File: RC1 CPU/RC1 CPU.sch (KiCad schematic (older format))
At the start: 42 parts, among them J1 Expansion, J2 RC1_UI_Port, J3 BARREL_JACK, M1 Mounting, M2 Mounting, M3 Mounting, M4 Mounting, U1 WD65C02, U2 HM62256BLP-7, U3 28C256, U4 6532, U5 74LS00, U6 LM556, U7 74LS145, U8 74LS138, U9 74LS00, X1 1MHz

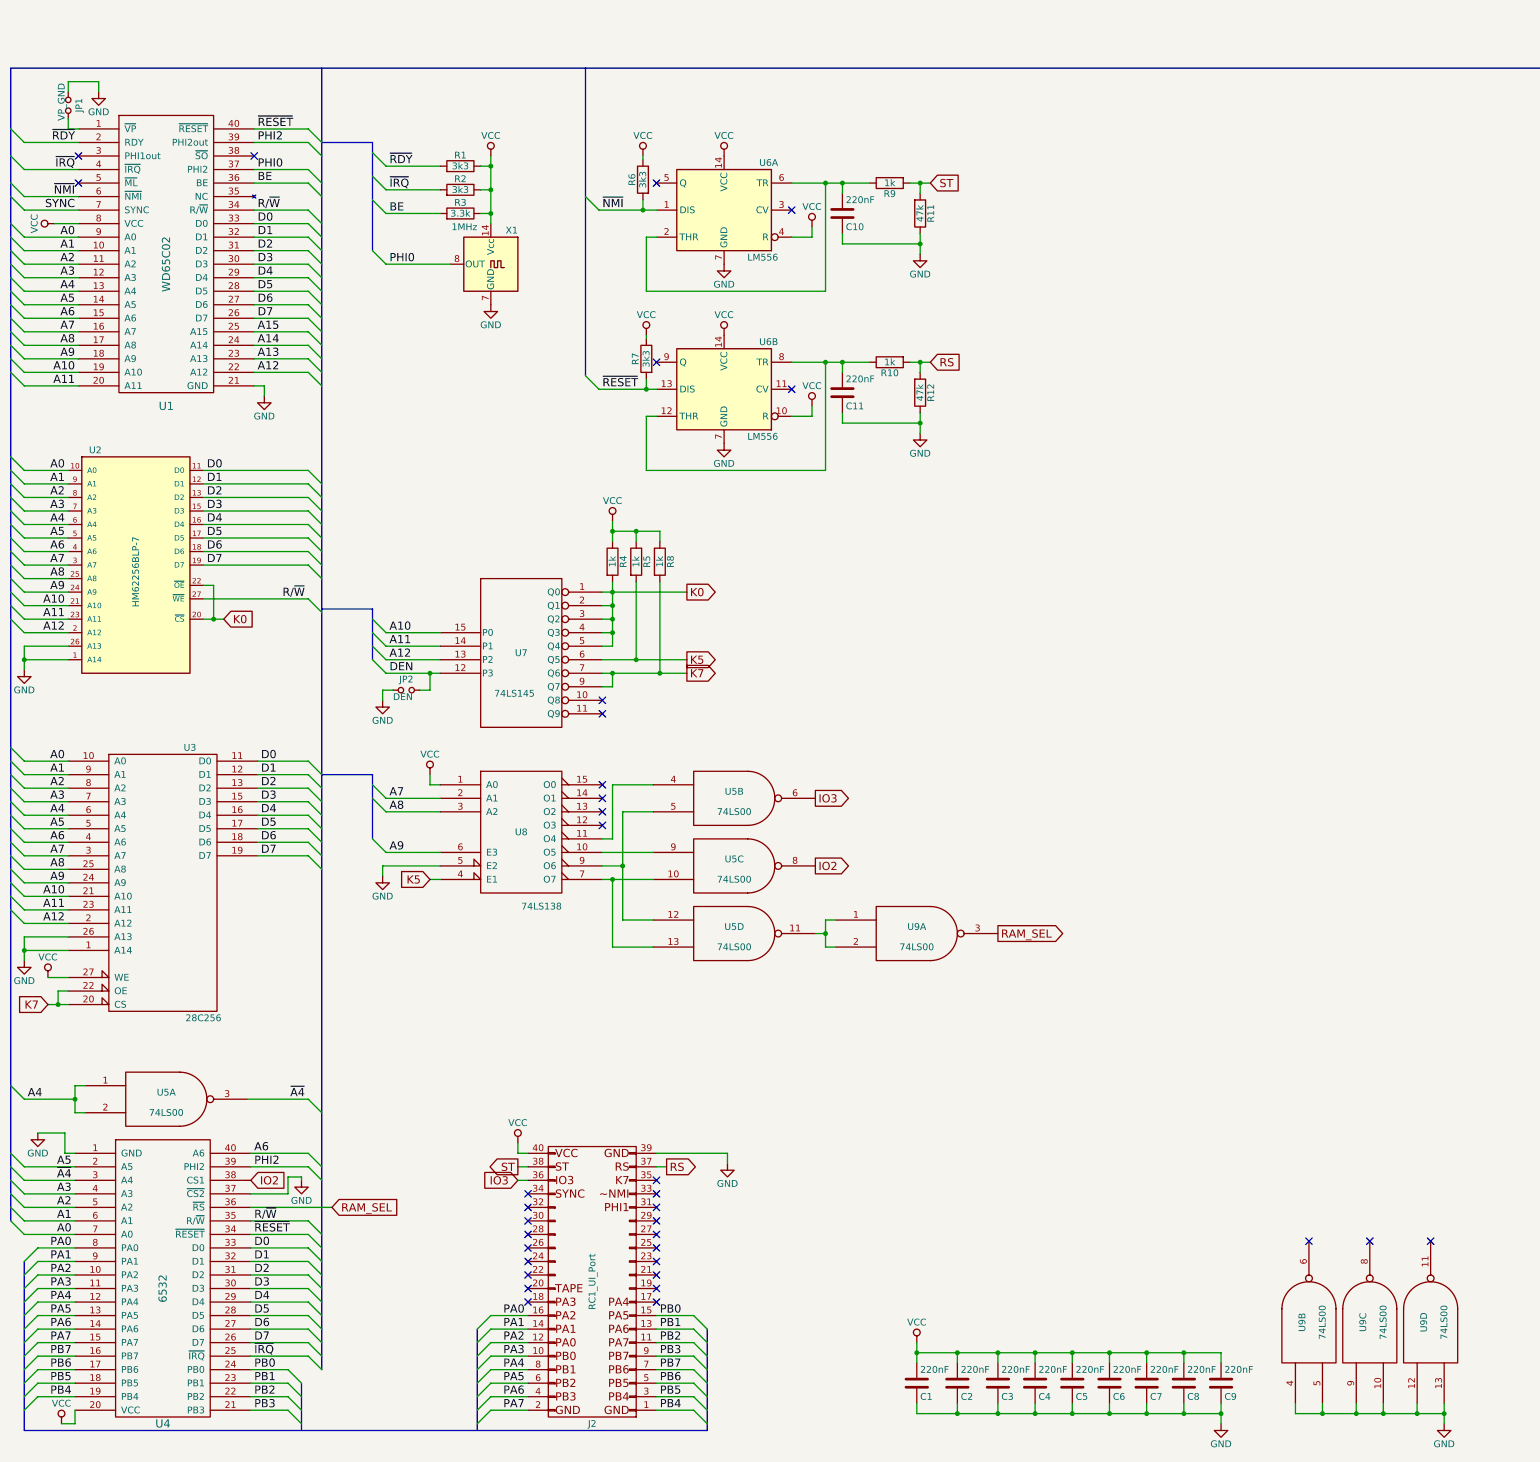
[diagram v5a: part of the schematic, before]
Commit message: Routed most signals on CPU board
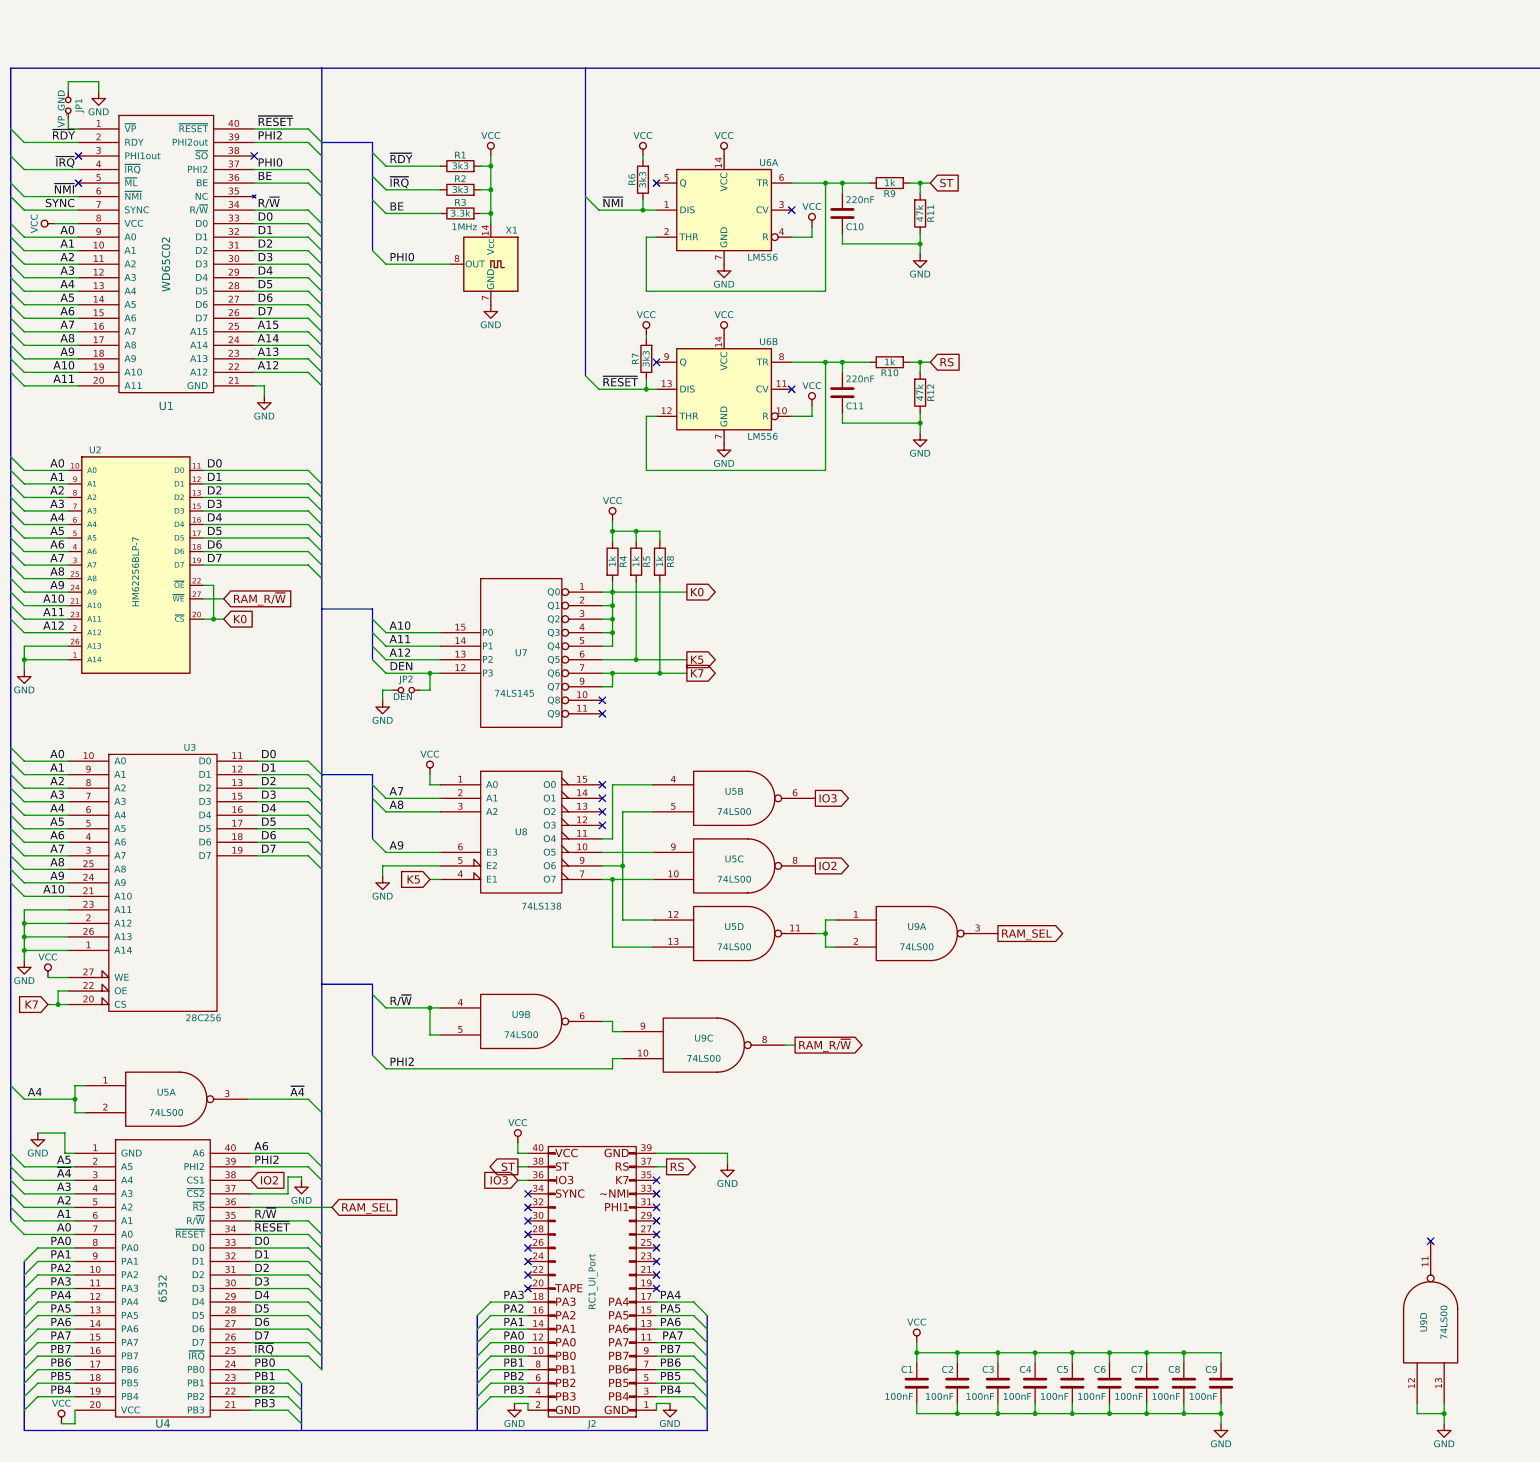
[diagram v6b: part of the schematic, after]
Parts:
- C1, C2, C3, C4, C5, C6, C7, C8, C9: value 220nF -> 100nF; footprint (none) -> Capacitors_THT:C_Disc_D4.7mm_W2.5mm_P5.00mm
- C10, C11: footprint (none) -> Capacitors_THT:C_Disc_D4.7mm_W2.5mm_P5.00mm
- JP1, JP2: footprint (none) -> Pin_Headers:Pin_Header_Straight_1x02_Pitch2.54mm
- R1, R10, R11, R12, R2, R3, R4, R5, R6, R7, R8, R9: footprint (none) -> Resistors_THT:R_Axial_DIN0207_L6.3mm_D2.5mm_P10.16mm_Horizontal
- U1, U4: footprint (none) -> Housings_DIP:DIP-40_W15.24mm_Socket
- U2: footprint DIP28 -> Housings_DIP:DIP-28_W15.24mm_Socket
- U3: footprint (none) -> Housings_DIP:DIP-28_W15.24mm_Socket
- U5, U6, U9: footprint (none) -> Housings_DIP:DIP-14_W7.62mm_Socket
- U7, U8: footprint (none) -> Housings_DIP:DIP-16_W7.62mm_Socket
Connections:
- net A11: no longer U3.23 (A11)
- net A12: no longer U3.2 (A12)
- net BE: now also R3.1; no longer R3.2
- net GND: now also C1.2, C2.2, C3.2, C4.2, C5.2, C6.2, C7.2, C8.2, C9.2, J2.1 (P1), J2.2 (P2), JP1.2, U3.2 (A12), U3.23 (A11); no longer C1.1, C2.1, C3.1, C4.1, C5.1, C6.1, C7.1, C8.1, C9.1, JP1.1, U9.10, U9.4, U9.5, U9.9
- net PA0: now also J2.12 (P12); no longer J2.16 (P16)
- net PA2: now also J2.16 (P16); no longer J2.12 (P12)
- net PA3: now also J2.18 (P18); no longer J2.10 (P10)
- net PA4: now also J2.17 (P17); no longer J2.8 (P8)
- net PA5: now also J2.15 (P15); no longer J2.6 (P6)
- net PA6: now also J2.13 (P13); no longer J2.4 (P4)
- net PA7: now also J2.11 (P11); no longer J2.2 (P2)
- net PB0: now also J2.10 (P10); no longer J2.15 (P15)
- net PB1: now also J2.8 (P8); no longer J2.13 (P13)
- net PB2: now also J2.6 (P6); no longer J2.11 (P11)
- net PB3: now also J2.4 (P4); no longer J2.9 (P9)
- net PB4: now also J2.3 (P3); no longer J2.1 (P1)
- net PB5: now also J2.5 (P5); no longer J2.3 (P3)
- net PB6: now also J2.7 (P7); no longer J2.5 (P5)
- net PB7: now also J2.9 (P9); no longer J2.7 (P7)
- net PHI2: now also U9.10
- net R/~W: now also U9.4, U9.5; no longer U2.27 (~WE)
- net VCC: now also C1.1, C2.1, C3.1, C4.1, C5.1, C6.1, C7.1, C8.1, C9.1, R1.2, R2.2, R3.2, R6.2, R7.2; no longer C1.2, C2.2, C3.2, C4.2, C5.2, C6.2, C7.2, C8.2, C9.2, R1.1, R2.1, R3.1, R6.1, R7.1
- net ~IRQ: now also R2.1; no longer R2.2
- net ~NMI: now also R6.1; no longer R6.2
- net ~RDY: now also R1.1; no longer R1.2
- net ~RESET: now also R7.1; no longer R7.2
- net at U1.1 (~VP): now also JP1.1; no longer JP1.2
- net at U9.6: now also U9.9
- net RAM_R/~W: now reaches U9.8
- net RAM_R/~W: now also U2.27 (~WE)
- no-connect marks 35 -> 31
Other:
- moved on the sheet: U9B, U9C

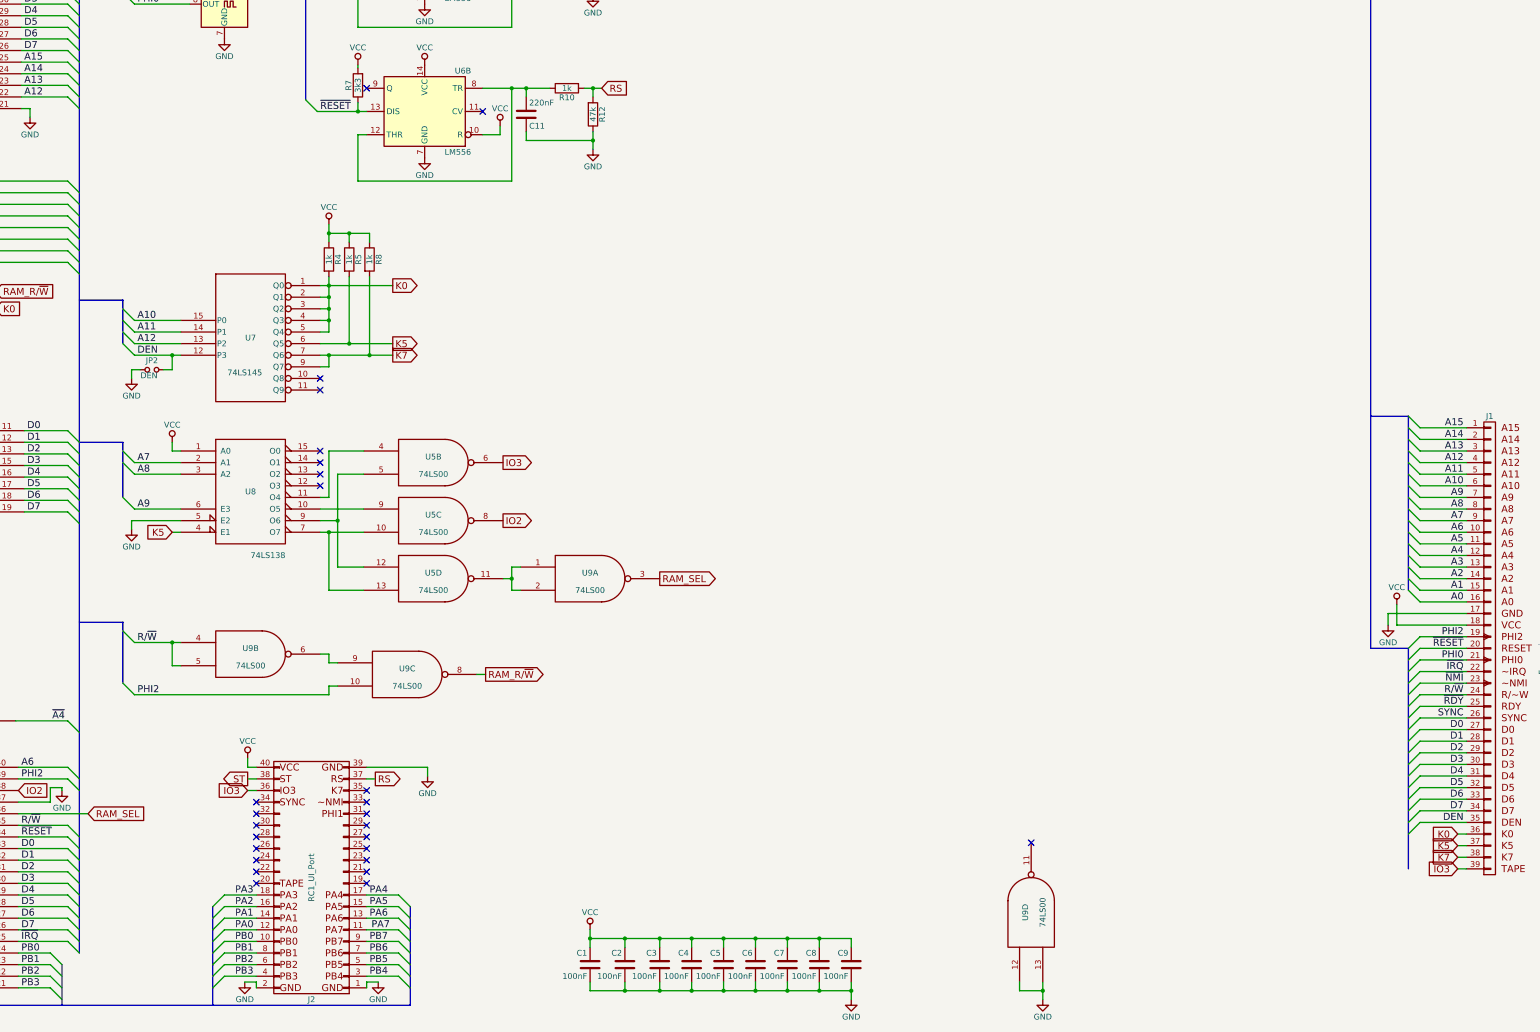
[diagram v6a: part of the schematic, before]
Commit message: Added UI signals to CPU board
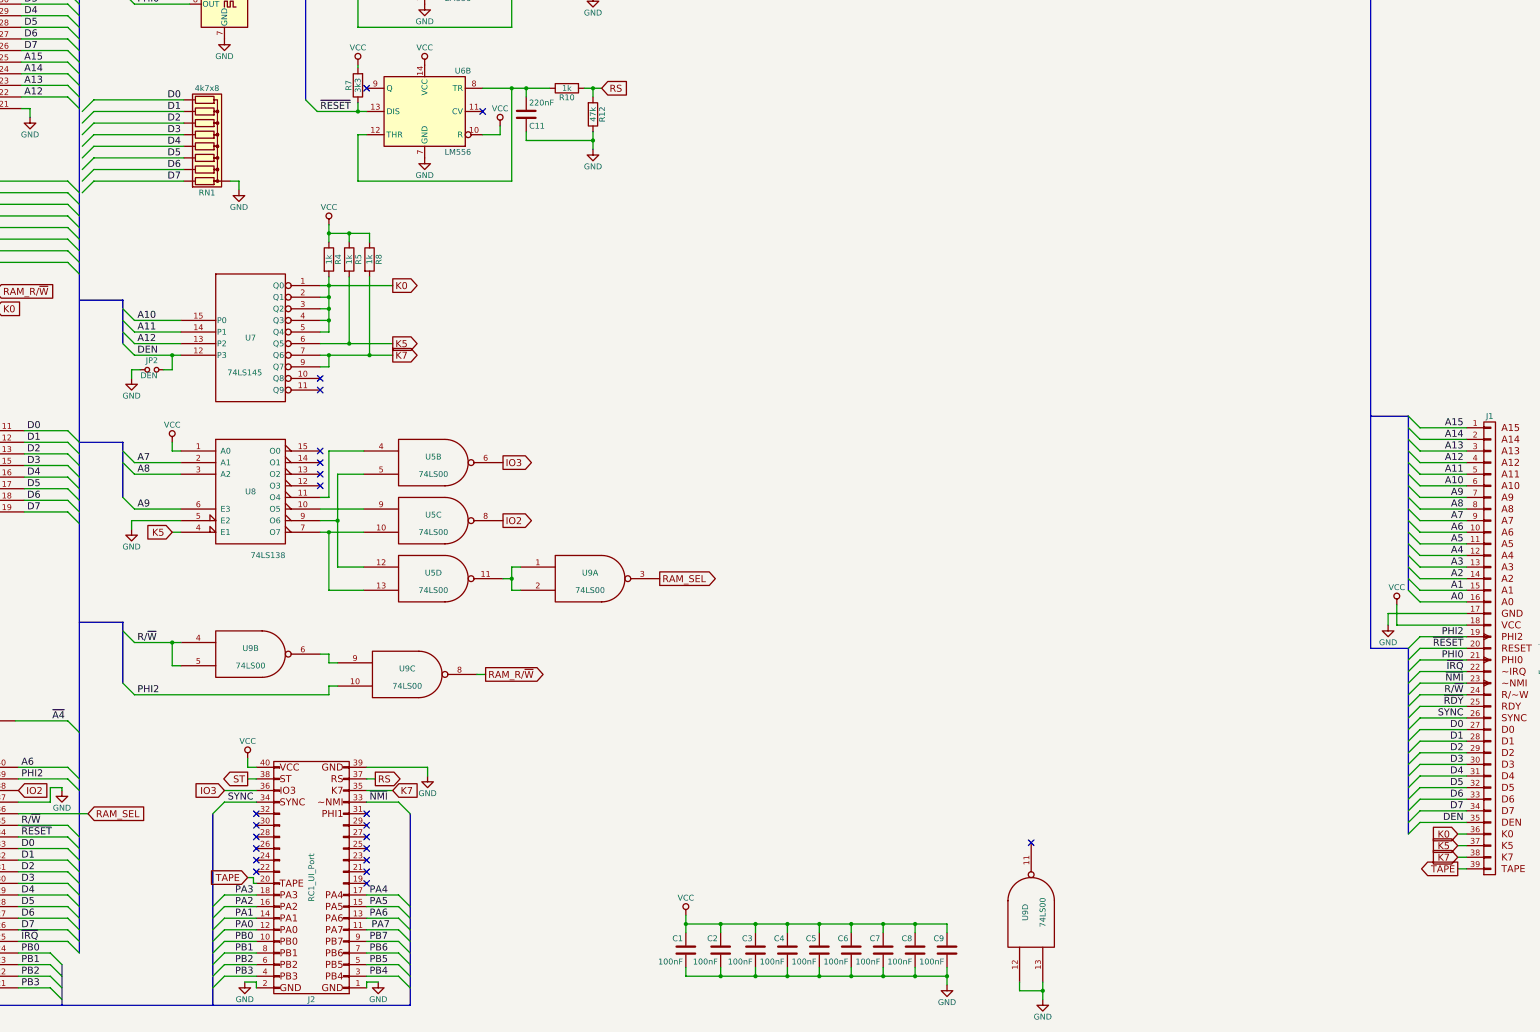
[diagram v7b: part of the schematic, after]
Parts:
- added RN1: 4k7x8, Resistors_THT:R_Array_SIP9, symbol R_Network08
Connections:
- net D0: now also RN1.9 (R8)
- net D1: now also RN1.8 (R7)
- net D2: now also RN1.7 (R6)
- net D3: now also RN1.6 (R5)
- net D4: now also RN1.5 (R4)
- net D5: now also RN1.4 (R3)
- net D6: now also RN1.3 (R2)
- net D7: now also RN1.2 (R1)
- net GND: now also RN1.1 (common)
- net IO3: no longer J1.39 (P39)
- net K7: now also J2.35 (P35)
- net SYNC: now also J2.34 (P34)
- net ~NMI: now also J2.33 (P33)
- net TAPE: now reaches J2.20 (P20)
- net TAPE: now also J1.39 (P39)
- no-connect marks 31 -> 27
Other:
- moved on the sheet: C1, C2, C3, C4, C5, C6, C7, C8, C9
